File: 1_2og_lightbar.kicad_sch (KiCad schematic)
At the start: 35 parts, among them J1 Conn_01x03

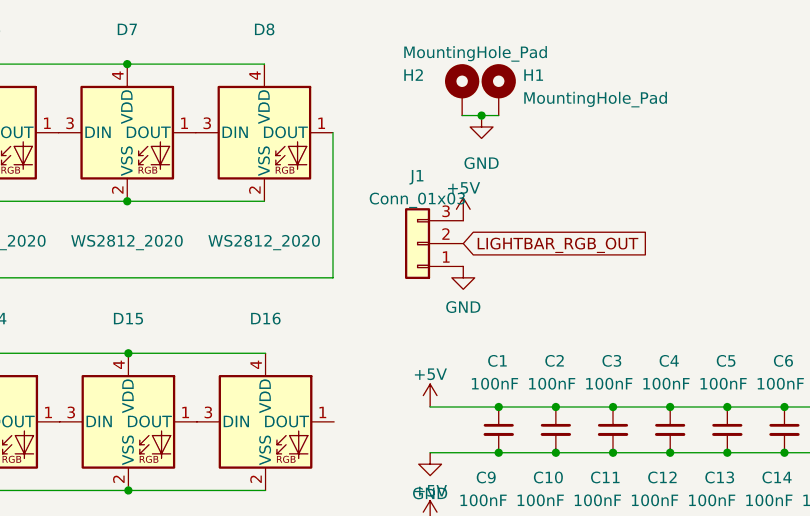
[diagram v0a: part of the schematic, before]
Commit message: add lightbar kinda (gerbers have not been fully updated yet, bom is broken)
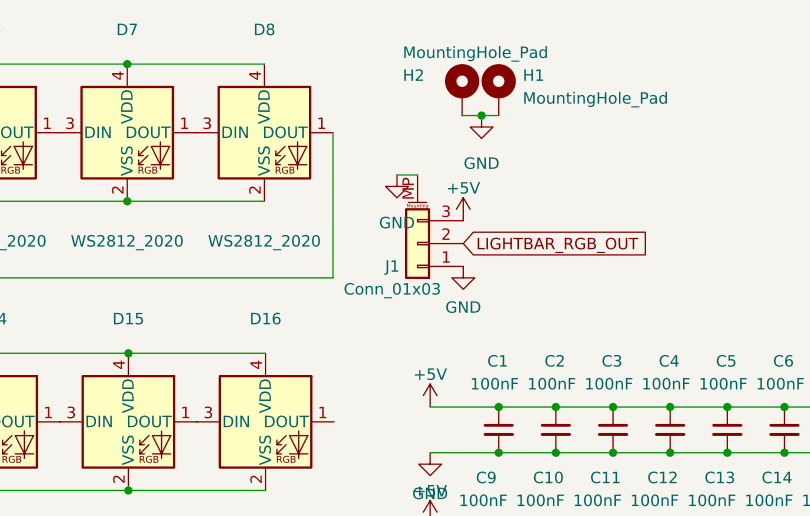
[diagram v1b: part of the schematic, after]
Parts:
- J1: footprint Connector_PinHeader_2.00mm:PinHeader_1x03_P2.00mm_Vertical -> Connector_Molex:Molex_Pico-EZmate_78171-0003_1x03-1MP_P1.20mm_Vertical; symbol Connector_Generic:Conn_01x03 -> Connector_Generic_MountingPin:Conn_01x03_MountingPin
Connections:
- net GND: now also J1.MP (MountPin)
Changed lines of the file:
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@@
+    (stroke (width 0) (type default))
+  )
+  (wire (pts (xy 157.607 31.115) (xy 159.893 31.115))
     (stroke (width 0) (type default))
   )
@@
     )
   )
+  (symbol (lib_name "GND_1") (lib_id "power:GND") (at 157.607 31.115 0) (unit 1)
+    (in_bom yes) (on_board yes) (dnp no) (fields_autoplaced)
+    (property "Reference" "#PWR05" (at 157.607 37.465 0)
+      (effects (font (size 1.27 1.27)) hide)
+    )
+    (property "Value" "GND" (at 157.607 36.449 0)
+      (effects (font (size 1.27 1.27)))
+    )
+    (property "Footprint" "" (at 157.607 31.115 0)
+      (effects (font (size 1.27 1.27)) hide)
+    )
+    (property "Datasheet" "" (at 157.607 31.115 0)
+      (effects (font (size 1.27 1.27)) hide)
+    )
+    (pin "1")
+    (instances
+      (project "1_2og_lightbar"
+        (path "/b7d27113-f6cf-475e-bba4-2eec7f4a6a32"
+          (reference "#PWR05") (unit 1)
+        )
+      )
+    )
+  )
   (symbol (lib_id "Device:C_Small") (at 168.91 59.436 0) (unit 1)
     (in_bom yes) (on_board yes) (dnp no)
@@
     )
   )
-  (symbol (lib_id "Connector_Generic:Conn_01x03") (at 159.893 38.735 180) (unit 1)
-    (in_bom yes) (on_board yes) (dnp no) (fields_autoplaced)
-    (property "Reference" "J1" (at 159.893 31.242 0)
-      (effects (font (size 1.27 1.27)))
-    )
-    (property "Value" "Conn_01x03" (at 159.893 33.782 0)
-      (effects (font (size 1.27 1.27)))
-    )
-    (property "Footprint" "Connector_PinHeader_2.00mm:PinHeader_1x03_P2.00mm_Vertical" (at 159.893 38.735 0)
+  (symbol (lib_id "Connector_Generic_MountingPin:Conn_01x03_MountingPin") (at 159.893 38.735 180) (unit 1)
+    (in_bom yes) (on_board yes) (dnp no)
+    (property "Reference" "J1" (at 157.099 41.275 0)
+      (effects (font (size 1.27 1.27)))
+    )
+    (property "Value" "Conn_01x03" (at 157.099 43.815 0)
+      (effects (font (size 1.27 1.27)))
+    )
+    (property "Footprint" "Connector_Molex:Molex_Pico-EZmate_78171-0003_1x03-1MP_P1.20mm_Vertical" (at 159.893 38.735 0)
       (effects (font (size 1.27 1.27)) hide)
     )
@@
     (pin "2")
     (pin "3")
-    (instances
-      (project "1_2og_lightbar"
+    (pin "MP")
+    (instances
+      (project "1_2og_lightbar"
